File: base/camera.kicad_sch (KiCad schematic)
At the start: 19 parts, among them J13 fan, J2 Conn_01x20, J9 spindle, Q1 Q_NMOS_GDS_spindle, Q2 Q_NMOS_GDS_fan

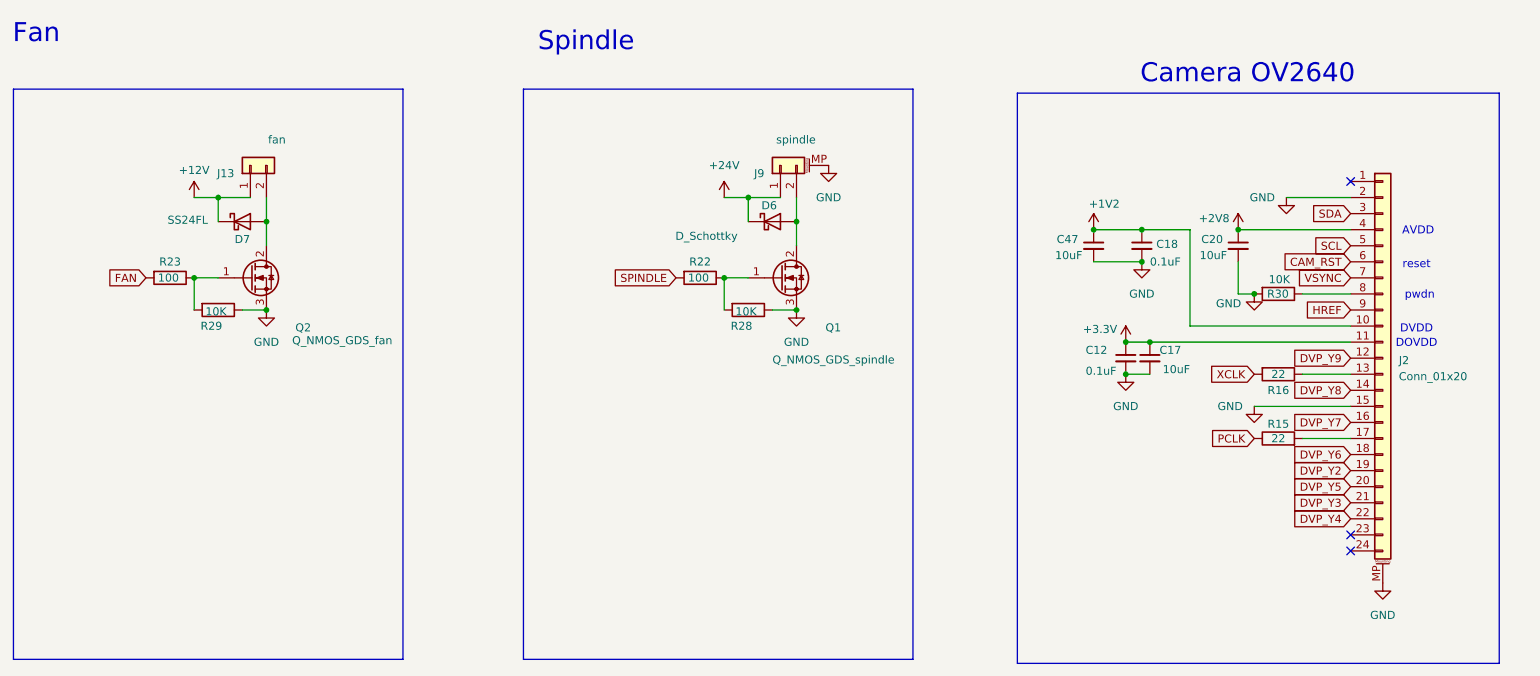
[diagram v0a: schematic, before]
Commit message: improved powernet, fixed bugs, tuned tracks for camera
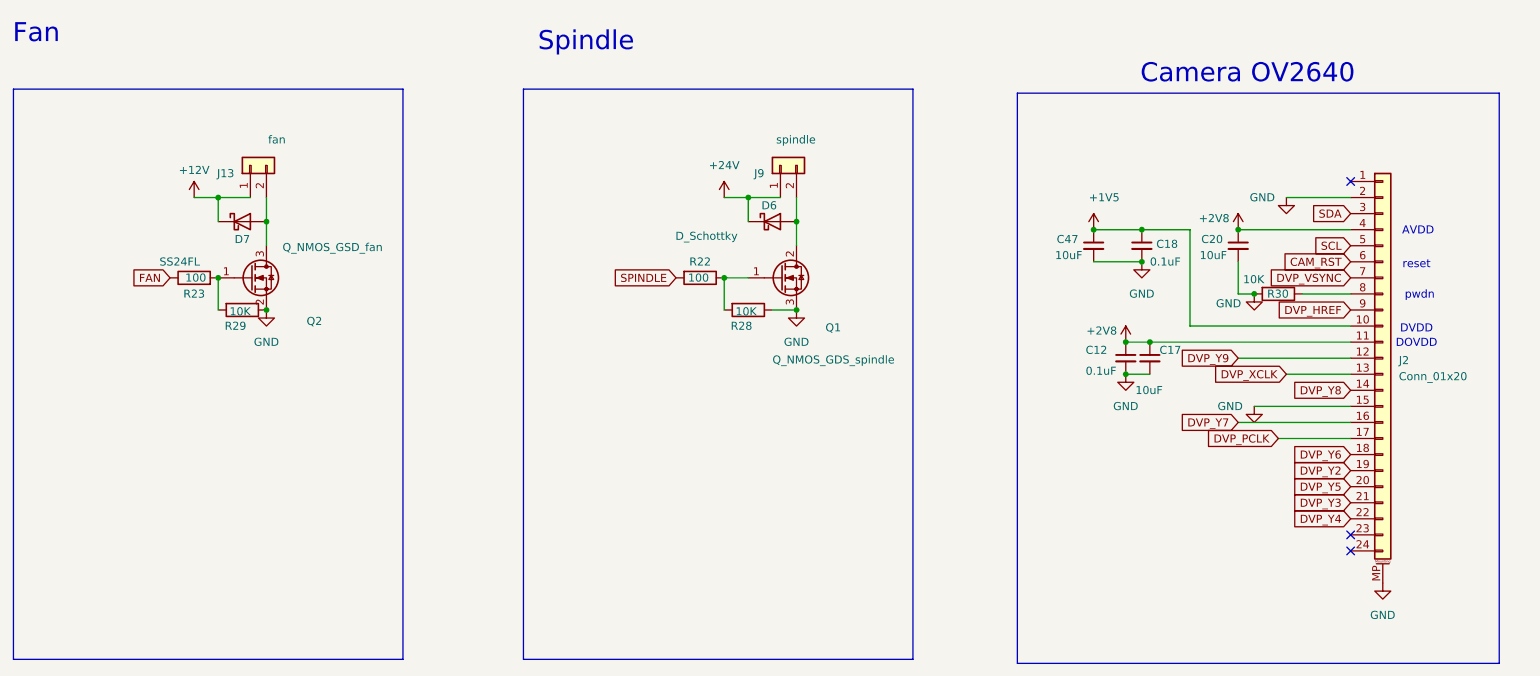
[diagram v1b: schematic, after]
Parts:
- removed R15, R16: 22, Resistor_SMD:R_0805_2012Metric, symbol Device:R
- J13: footprint footprints:TSM-102-01-L-SV -> footprints:JST_B2B-XH-A_LF__SN_
- J9: footprint footprints:21548291 -> footprints:JST_VH_B2P-VH_1x02_P3.96mm_Vertical; symbol Connector_Generic_MountingPin:Conn_01x02_MountingPin -> Connector_Generic:Conn_01x02; farnell# 4299228 -> 9492003; manf# 2154829-1 -> B2P-VH; mouser# 571-2154829-1 -> 306-B2P-VHLFSN
- Q2: value Q_NMOS_GDS_fan -> Q_NMOS_GSD_fan; symbol Transistor_FET:Q_NMOS_GDS -> Transistor_FET:Q_NMOS_GSD
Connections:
- net +3.3V is gone; now on net +2V8: C12.1, C17.1, J2.11 (Pin_11)
- net FAN: now also R23.1; no longer R23.2
- net GND: now also Q2.2 (S); no longer J9.MP (MountPin), Q2.3 (S)
- net DVP_XCLK: now reaches J2.13 (Pin_13)
- net at Q2.1 (G), R29.2: now also R23.2; no longer R23.1
- net at D7.2 (A), J13.2 (Pin_2): now also Q2.3 (D); no longer Q2.2 (D)
- net DVP_PCLK: now reaches J2.17 (Pin_17)
- net +1V2 renamed +1V5
- net HREF renamed DVP_HREF
- net VSYNC renamed DVP_VSYNC
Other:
- moved on the sheet: R23, R29

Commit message: send to fab
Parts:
- J13: mouser# 200-TSM10201TSV -> 863-BZX84C12LT1G
- J2: value Conn_01x20 -> FPC-24P-0.5mm
- J9: mouser# 306-B2P-VHLFSN -> 306-B2PVHBKLFSN
- Q1: farnell# 1752049 -> 2101407; manf# STD120N4LF6 -> FDD8447L; mouser# 511-STD120N4LF6 -> 512-FDD8447L
- R28, R29, R30: value 10K -> 5.1K; farnell# 2826162 -> 1469937; manf# CRCW080510K0JNEAC -> CRCW08055K10FKEA; mouser# 71-CRCW080510K0JNEAC -> -71-CRCW0805-5.1K-E3
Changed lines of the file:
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@@
 		(dnp no)
 		(property "Reference" "R30"
-			(at 243.332 74.93 90)
+			(at 239.522 72.898 90)
 			(show_name no)
 			(do_not_autoplace no)
@@
 			)
 		)
-		(property "Value" "10K"
-			(at 239.522 72.644 90)
+		(property "Value" "5.1K"
+			(at 243.078 75.184 90)
 			(show_name no)
 			(do_not_autoplace no)
@@
 			)
 		)
-		(property "farnell#" "2826162"
+		(property "farnell#" "1469937"
 			(at 245.11 74.93 0)
 			(hide yes)
@@
 			)
 		)
-		(property "manf#" "CRCW080510K0JNEAC"
+		(property "manf#" "CRCW08055K10FKEA"
 			(at 245.11 74.93 0)
 			(hide yes)
@@
 			)
 		)
-		(property "mouser#" "71-CRCW080510K0JNEAC"
+		(property "mouser#" "-71-CRCW0805-5.1K-E3"
 			(at 245.11 74.93 0)
 			(hide yes)
@@
 			)
 		)
-		(property "mouser#" "511-STD120N4LF6"
+		(property "mouser#" "512-FDD8447L"
 			(at 166.37 72.39 0)
 			(hide yes)
@@
 			)
 		)
-		(property "farnell#" "1752049"
+		(property "farnell#" "2101407"
 			(at 166.37 72.39 0)
 			(hide yes)
@@
 			)
 		)
-		(property "manf#" "STD120N4LF6"
+		(property "manf#" "FDD8447L"
 			(at 166.37 72.39 0)
 			(hide yes)
@@
 			)
 		)
-		(property "Value" "10K"
+		(property "Value" "5.1K"
 			(at 79.248 77.724 90)
 			(show_name no)
@@
 			)
 		)
-		(property "farnell#" "2826162"
+		(property "farnell#" "1469937"
 			(at 81.28 77.47 0)
 			(hide yes)
@@
 			)
 		)
-		(property "manf#" "CRCW080510K0JNEAC"
+		(property "manf#" "CRCW08055K10FKEA"
 			(at 81.28 77.47 0)
 			(hide yes)
@@
 			)
 		)
-		(property "mouser#" "71-CRCW080510K0JNEAC"
+		(property "mouser#" "-71-CRCW0805-5.1K-E3"
 			(at 81.28 77.47 0)
 			(hide yes)
@@
 			)
 		)
-		(property "mouser#" "200-TSM10201TSV "
+		(property "mouser#" "863-BZX84C12LT1G"
 			(at 82.55 54.61 90)
 			(hide yes)
@@
 			)
 		)
-		(property "Value" "Conn_01x20"
+		(property "Value" "FPC-24P-0.5mm"
 			(at 264.16 87.9855 0)
 			(show_name no)
@@
 			)
 		)
-		(property "mouser#" "306-B2P-VHLFSN "
+		(property "mouser#" "306-B2PVHBKLFSN"
 			(at 166.37 54.61 90)
 			(hide yes)
@@
 			)
 		)
-		(property "Value" "10K"
+		(property "Value" "5.1K"
 			(at 159.258 77.724 90)
 			(show_name no)
@@
 			)
 		)
-		(property "farnell#" "2826162"
+		(property "farnell#" "1469937"
 			(at 161.29 77.47 0)
 			(hide yes)
@@
 			)
 		)
-		(property "manf#" "CRCW080510K0JNEAC"
+		(property "manf#" "CRCW08055K10FKEA"
 			(at 161.29 77.47 0)
 			(hide yes)
@@
 			)
 		)
-		(property "mouser#" "71-CRCW080510K0JNEAC"
+		(property "mouser#" "-71-CRCW0805-5.1K-E3"
 			(at 161.29 77.47 0)
 			(hide yes)

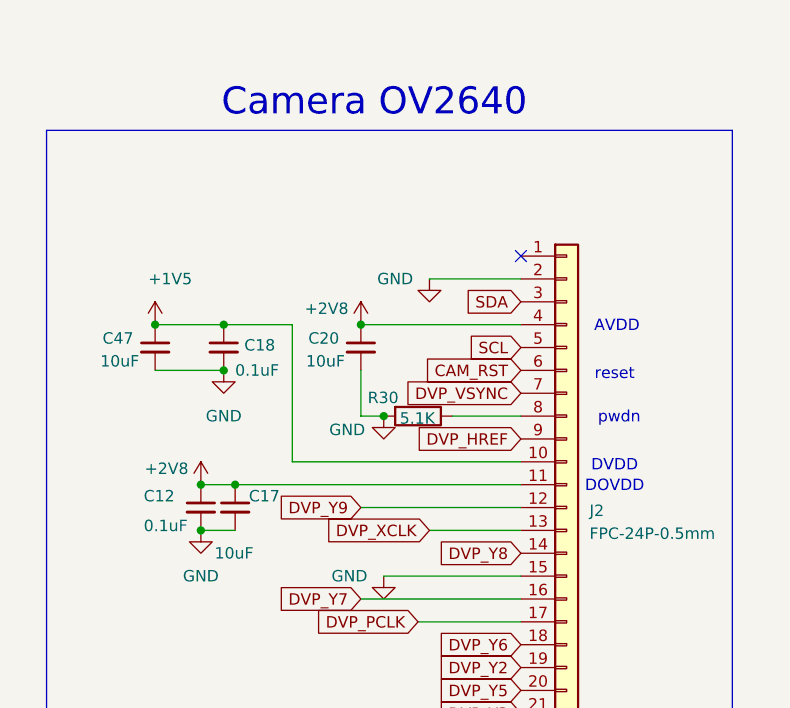
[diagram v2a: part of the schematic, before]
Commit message: fixed: uartx res to 5.1K, switch connection cross, camera connextor top side
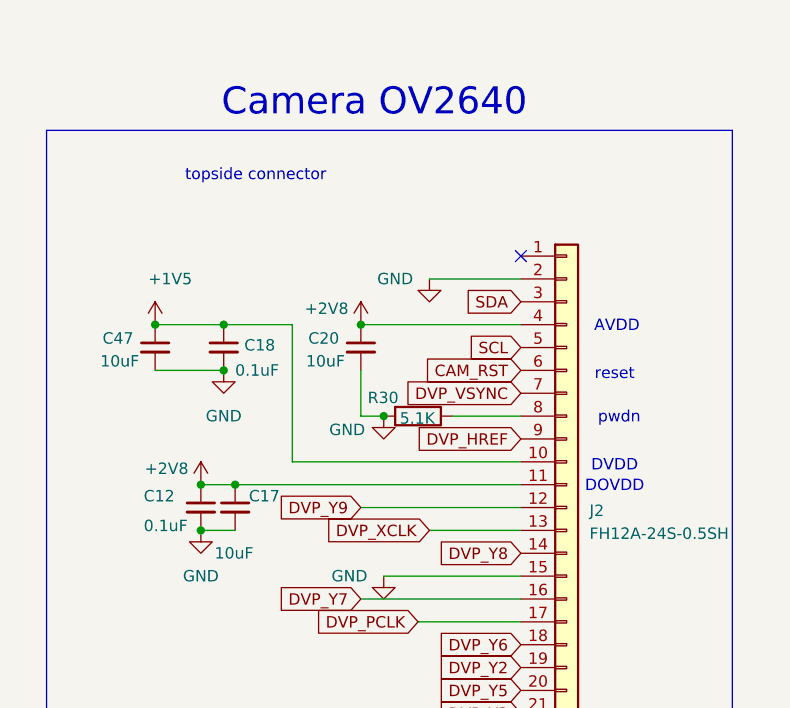
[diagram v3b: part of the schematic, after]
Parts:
- J13: farnell# 3662696 -> 3287572; manf# TSM-102-01-T-SV -> B2B-XH-A (LF)(SN); mouser# 863-BZX84C12LT1G -> 306-B2BXHALFSNP
- J2: value FPC-24P-0.5mm -> FH12A-24S-0.5SH; farnell# 1324552 -> 1324565; manf# FH12-24S-0.5SH(55) -> FH12A-24S-0.5SH; mouser# 798-FH12-24S-0.5SH55 -> 798-FH12A-24S0.5SH55; notes kan 10 bit uitzenden, maar dat is te veel info -> (none)
- R22, R23: footprint Resistor_SMD:R_0805_2012Metric_Pad1.20x1.40mm_HandSolder -> Resistor_SMD:R_0805_2012Metric
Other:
- note added: "topside connector"
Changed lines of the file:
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@@
 		)
 	)
+	(text "topside connector"
+		(exclude_from_sim no)
+		(at 227.076 48.26 0)
+		(effects
+			(font
+				(size 1.27 1.27)
+			)
+		)
+	)
 	(text "reset"
 		(exclude_from_sim no)
@@
 			)
 		)
-		(property "mouser#" "863-BZX84C12LT1G"
+		(property "mouser#" "306-B2BXHALFSNP"
 			(at 82.55 54.61 90)
 			(hide yes)
@@
 			)
 		)
-		(property "manf#" "TSM-102-01-T-SV "
+		(property "manf#" "B2B-XH-A (LF)(SN)"
 			(at 82.55 54.61 90)
 			(hide yes)
@@
 			)
 		)
-		(property "farnell#" "3662696"
+		(property "farnell#" "3287572"
 			(at 82.55 54.61 90)
 			(hide yes)
@@
 			)
 		)
-		(property "Footprint" "Resistor_SMD:R_0805_2012Metric_Pad1.20x1.40mm_HandSolder"
+		(property "Footprint" "Resistor_SMD:R_0805_2012Metric"
 			(at 73.66 74.168 90)
 			(hide yes)
@@
 			)
 		)
-		(property "Value" "FPC-24P-0.5mm"
+		(property "Value" "FH12A-24S-0.5SH"
 			(at 264.16 87.9855 0)
 			(show_name no)
@@
 			)
 		)
-		(property "manf#" "FH12-24S-0.5SH(55)"
+		(property "manf#" "FH12A-24S-0.5SH"
 			(at 261.62 85.09 0)
 			(hide yes)
@@
 			)
 		)
-		(property "farnell#" "1324552"
+		(property "farnell#" "1324565"
 			(at 261.62 85.09 0)
 			(hide yes)
@@
 			)
 		)
-		(property "mouser#" " 798-FH12-24S-0.5SH55"
+		(property "mouser#" "798-FH12A-24S0.5SH55"
 			(at 261.62 85.09 0)
 			(hide yes)
@@
 			)
 		)
-		(property "notes" "kan 10 bit uitzenden, maar dat is te veel info"
-			(at 261.62 85.09 0)
-			(hide yes)
-			(show_name no)
-			(do_not_autoplace no)
-			(effects
-				(font
-					(size 1.27 1.27)
-				)
-			)
-		)
 		(pin "5"
 		)
@@
 			)
 		)
-		(property "Footprint" "Resistor_SMD:R_0805_2012Metric_Pad1.20x1.40mm_HandSolder"
+		(property "Footprint" "Resistor_SMD:R_0805_2012Metric"
 			(at 153.67 70.612 90)
 			(hide yes)
